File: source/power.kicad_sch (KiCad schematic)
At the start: 135 parts, among them Q1 MMBT5401, Q10 MMBT5401, Q11 CSD19536KCS, Q12 CSD19536KCS, Q2 MMBT5401, Q3 CSD19536KCS, Q4 CSD19536KCS, Q5 MMBT5401, Q6 MMBT5401, Q7 CSD19536KCS, Q8 CSD19536KCS, Q9 MMBT5401, U11 MS8311, U12 MS8311, U13 MS8311

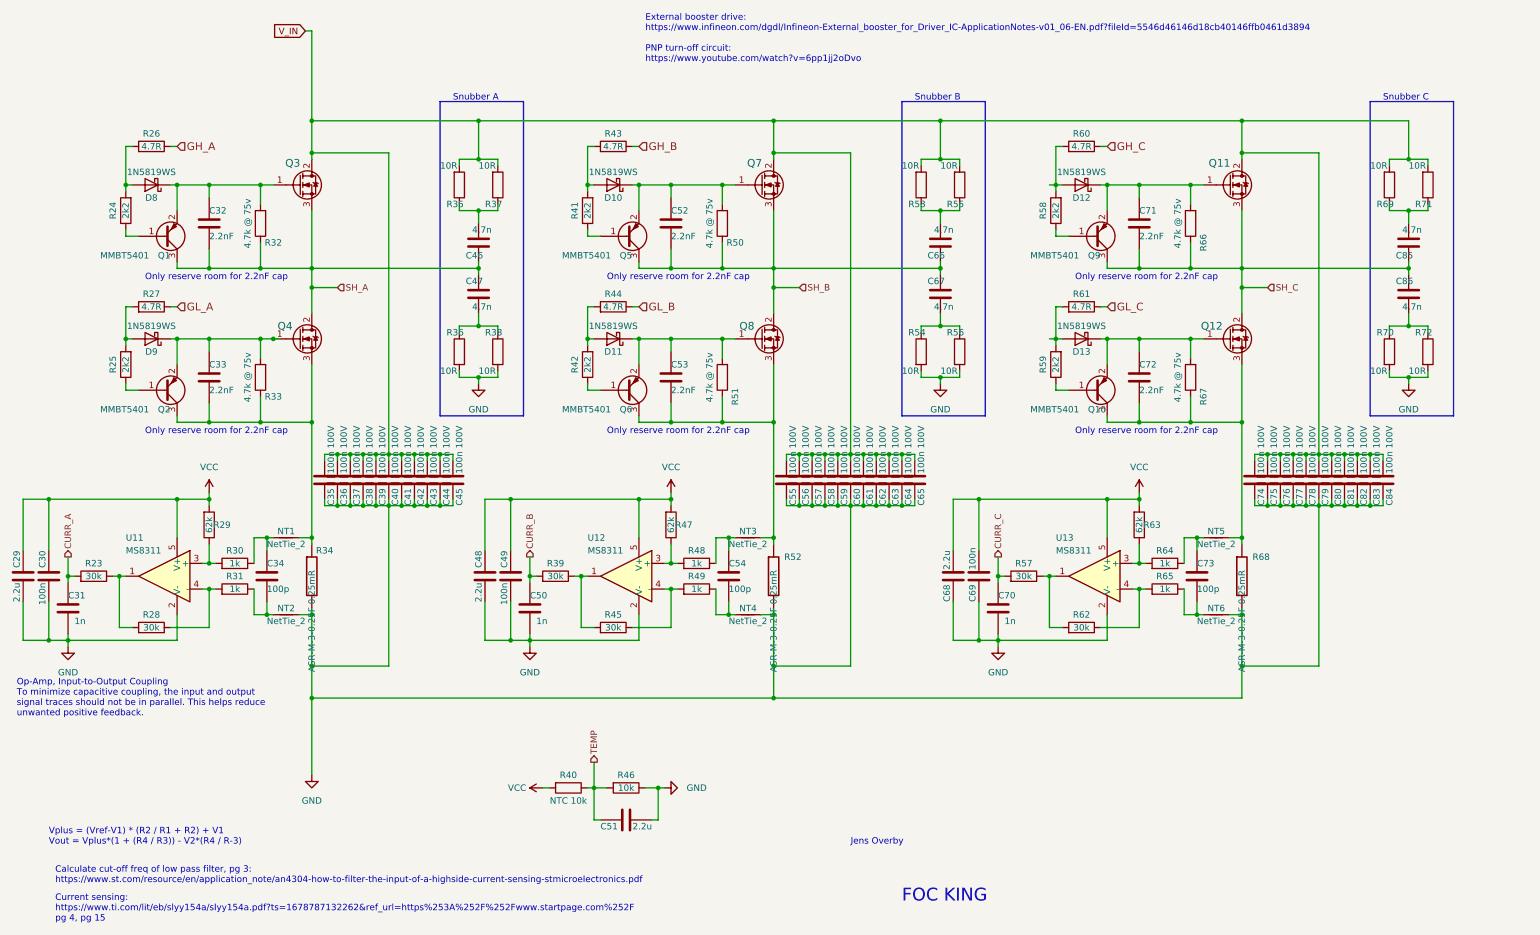
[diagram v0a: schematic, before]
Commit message: 4 layer design
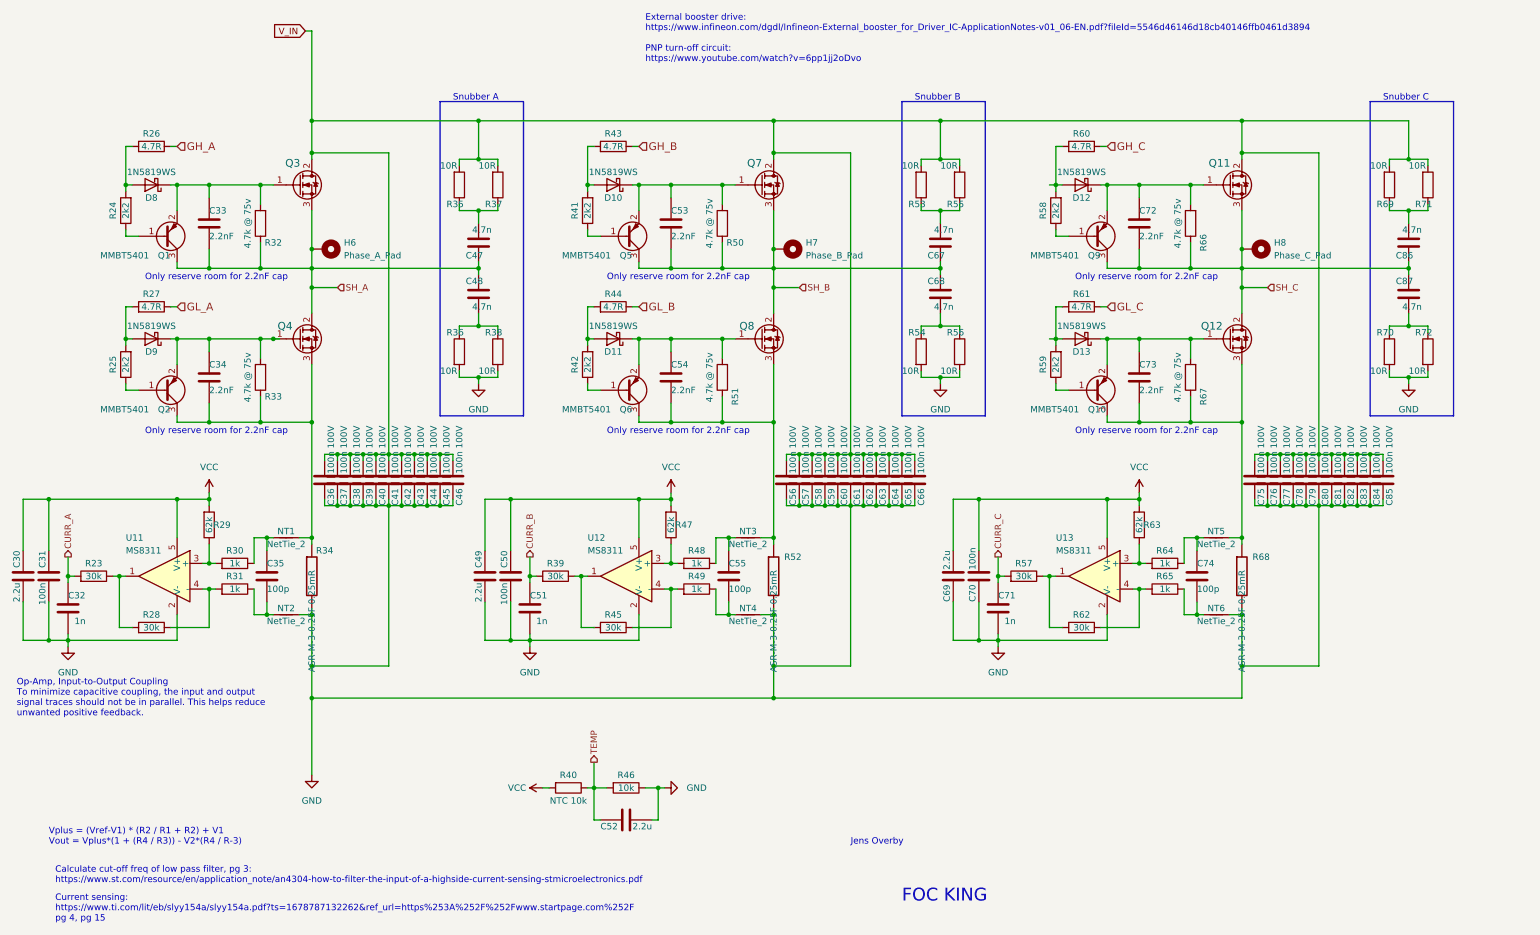
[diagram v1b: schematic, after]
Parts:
- added H6: Phase_A_Pad, Custom:MountingHole_3.5mm_Pad_TopOnly_custom, symbol Mechanical:MountingHole_Pad
- added H7: Phase_B_Pad, Custom:MountingHole_3.5mm_Pad_TopOnly_custom, symbol Mechanical:MountingHole_Pad
- added H8: Phase_C_Pad, Custom:MountingHole_3.5mm_Pad_TopOnly_custom, symbol Mechanical:MountingHole_Pad
- Q11, Q12, Q3, Q4, Q7, Q8: footprint Package_TO_SOT_THT:TO-220-3_Vertical -> Custom:TO-220-3_Vertical_bend
- renumbered C29 to C30, C30 to C31, C31 to C32, C32 to C33, C33 to C34, C34 to C35, C35 to C36, C36 to C37, C37 to C38, C38 to C39, C39 to C40, C40 to C41, C41 to C42, C42 to C43, C43 to C44, C44 to C45, C45 to C46, C46 to C47, C47 to C48, C48 to C49, C49 to C50, C50 to C51, C51 to C52, C52 to C53, C53 to C54, C54 to C55, C55 to C56, C56 to C57, C57 to C58, C58 to C59, C59 to C60, C60 to C61, C61 to C62, C62 to C63, C63 to C64, C64 to C65, C65 to C66, C66 to C67, C67 to C68, C68 to C69, C69 to C70, C70 to C71, C71 to C72, C72 to C73, C73 to C74, C74 to C75, C75 to C76, C76 to C77, C77 to C78, C78 to C79, C79 to C80, C80 to C81, C81 to C82, C82 to C83, C83 to C84, C84 to C85, C85 to C86, C86 to C87
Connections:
- net SH_A: now also H6.1
- net SH_B: now also H7.1
- net SH_C: now also H8.1

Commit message: Add files via upload
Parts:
- removed C33, C34, C53, C54, C72, C73: 2.2nF, Capacitor_SMD:C_0603_1608Metric, symbol BLDC_4-rescue:C-RESCUE-BLDC_4
- removed R32, R33, R50, R51, R66, R67: 4.7k @ 75v, Resistor_SMD:R_0603_1608Metric, symbol Device:R
- Q11, Q12, Q3, Q4, Q7, Q8: value CSD19536KCS -> CRST030N10N; footprint Custom:TO-220-3_Vertical_bend -> (none); LCSC (none) -> C841369
- R24: value 2k2 -> 0R; LCSC C22975 -> C21189
- R25: value 2k2 -> 2.2R; LCSC C22975 -> C22939
- R27: value 4.7R -> 2.2R; LCSC C23164 -> C22939
- R39: renamed from R41; value 2k2 -> 0R; LCSC C22975 -> C21189
- R40: renamed from R42; value 2k2 -> 2.2R; LCSC C22975 -> C22939
- R42: renamed from R44; value 4.7R -> 2.2R; LCSC C23164 -> C22939
- R54: renamed from R58; value 2k2 -> 0R; LCSC C22975 -> C21189
- R55: renamed from R59; value 2k2 -> 2.2R; LCSC C22975 -> C22939
- R57: renamed from R61; value 4.7R -> 2.2R; LCSC C23164 -> C22939
- renumbered C35 to C33, C36 to C34, C37 to C35, C38 to C36, C39 to C37, C40 to C38, C41 to C39, C42 to C40, C43 to C41, C44 to C42, C45 to C43, C46 to C44, C47 to C45, C48 to C46, C49 to C47, C50 to C48, C51 to C49, C52 to C50, C55 to C51, C56 to C52, C57 to C53, C58 to C54, C59 to C55, C60 to C56, C61 to C57, C62 to C58, C63 to C59, C64 to C60, C65 to C61, C66 to C62, C67 to C63, C68 to C64, C69 to C65, C70 to C66, C71 to C67, C74 to C68, C75 to C69, C76 to C70, C77 to C71, C78 to C72, C79 to C73, C80 to C74, C81 to C75, C82 to C76, C83 to C77, C84 to C78, C85 to C79, C86 to C80, C87 to C81, H6 to H5, H7 to H6, H8 to H7, R34 to R32, R35 to R33, R36 to R34, R37 to R35, R38 to R36, R39 to R37, R40 to R38, R43 to R41, R45 to R43, R46 to R44, R47 to R45, R48 to R46, R49 to R47, R52 to R48, R53 to R49, R54 to R50, R55 to R51, R56 to R52, R57 to R53, R60 to R56, R62 to R58, R63 to R59, R64 to R60, R65 to R61, R68 to R62, R69 to R63, R70 to R64, R71 to R65, R72 to R66
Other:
- note removed: "Only reserve room for 2.2nF cap"

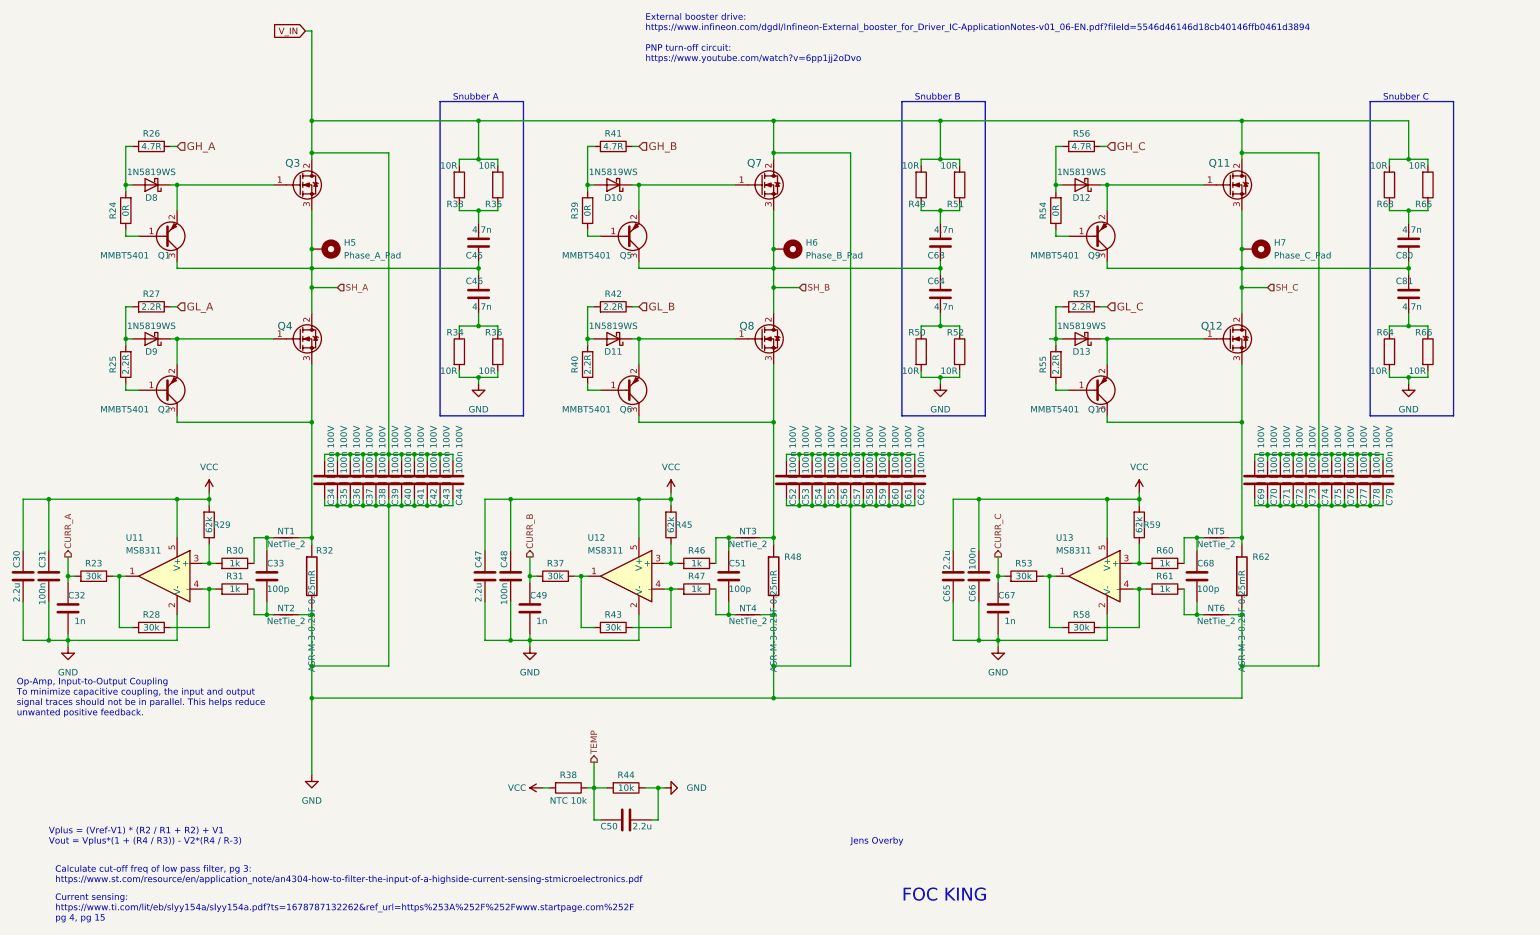
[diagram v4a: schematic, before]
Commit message: Add files via upload
Filter resistor on current op-amps changed from 30k to 150R
Mosfets at 45 deg angle
Changed layout of power supply
Cut through center of board
Unnecessary components near mosfets removed
Voltage filters removed again
Crystal suspected noise source - moved to back of board
Current sensing moved to in0 - in2 (PA0-PA2)
Voltage sensing moved to in11-in13
Supply voltage moved to in10
Mosfets can now be attached to heat-sink plate using screws (that can be tightened throug holes in the board)
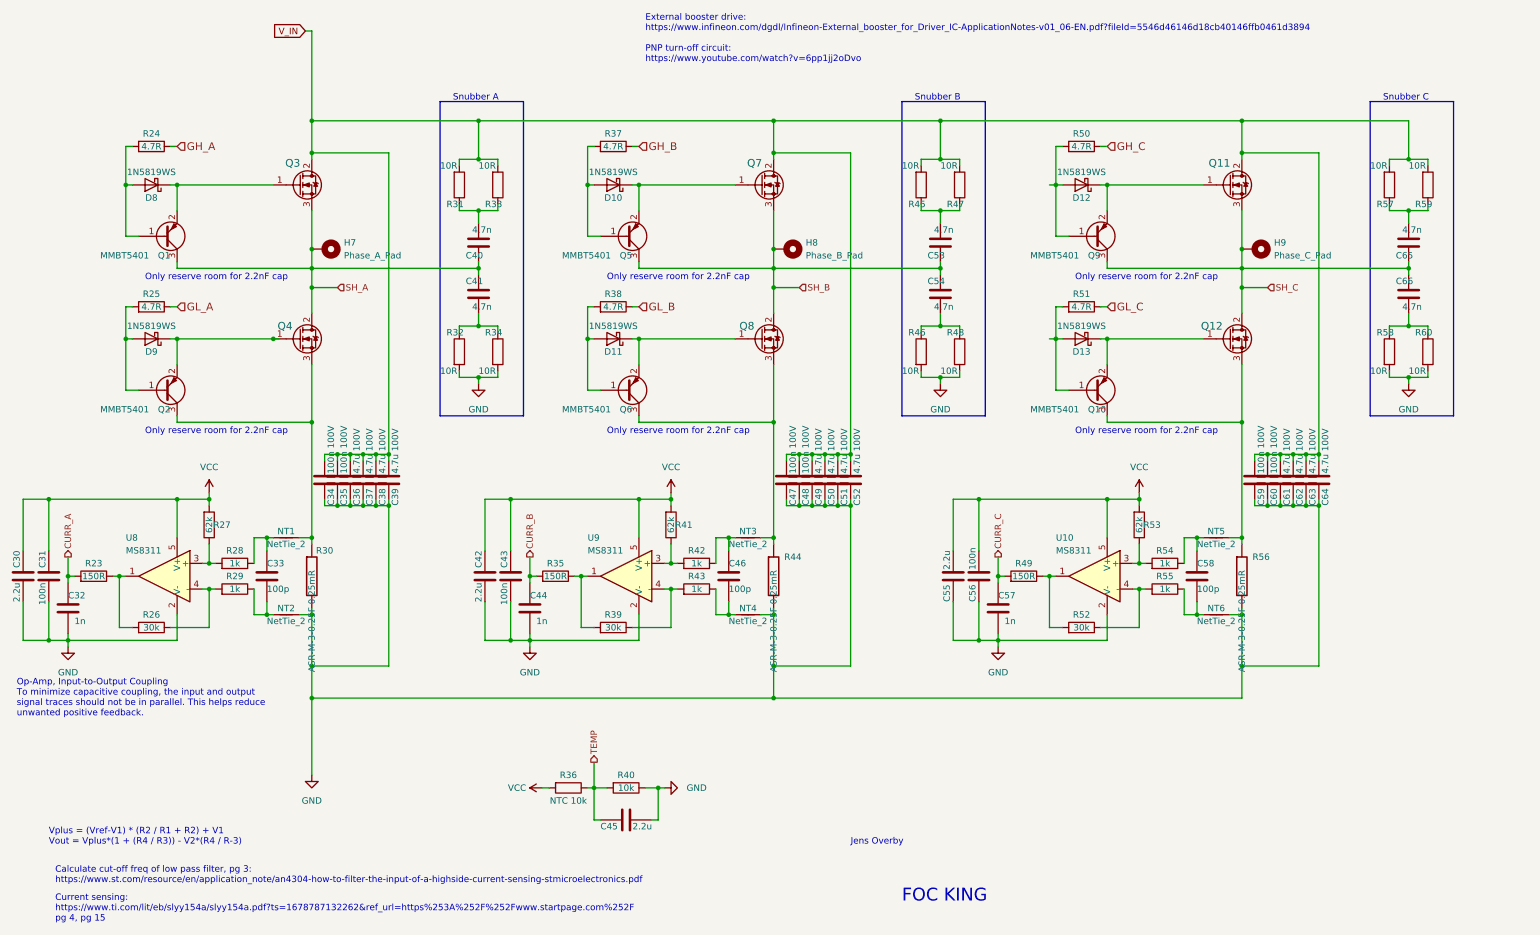
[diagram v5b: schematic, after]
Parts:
- removed C40, C41, C42, C43, C44, C53, C54, C55, C56, C57, C58, C69, C70, C71, C72, C73, C74, C75, C76, C77, C78, C79: 100n 100V, Capacitor_SMD:C_0805_2012Metric, symbol Device:C
- removed R24, R39, R54: 0R, Resistor_SMD:R_0603_1608Metric, symbol Device:R
- removed R25, R40, R55: 2.2R, Resistor_SMD:R_0603_1608Metric, symbol Device:R
- added C47, C48: 100n 100V, Capacitor_SMD:C_0805_2012Metric, symbol Device:C
- added C49, C50, C51, C63, C64: 4.7u 100V, Capacitor_SMD:C_1210_3225Metric, symbol Device:C
- C36, C37, C38, C39, C52, C61, C62: value 100n 100V -> 4.7u 100V; footprint Capacitor_SMD:C_0805_2012Metric -> Capacitor_SMD:C_1210_3225Metric; LRSC C28233 -> C381466
- Q11, Q12, Q3, Q4, Q7, Q8: value CRST030N10N -> CSD19536KCS; footprint (none) -> Custom:TO-220-3_Vertical_bend; LCSC C841369 -> (none)
- R23: value 30k -> 150R; LCSC C22984 -> C22808
- R25: renamed from R27; value 2.2R -> 4.7R; LCSC C22939 -> C23164
- R35: renamed from R37; value 30k -> 150R; LCSC C22984 -> C22808
- R38: renamed from R42; value 2.2R -> 4.7R; LCSC C22939 -> C23164
- R49: renamed from R53; value 30k -> 150R; LCSC C22984 -> C22808
- R51: renamed from R57; value 2.2R -> 4.7R; LCSC C22939 -> C23164
- renumbered C45 to C40, C46 to C41, C47 to C42, C48 to C43, C49 to C44, C50 to C45, C51 to C46, C63 to C53, C64 to C54, C65 to C55, C66 to C56, C67 to C57, C68 to C58, C80 to C65, C81 to C66, H5 to H7, H6 to H8, H7 to H9, R26 to R24, R28 to R26, R29 to R27, R30 to R28, R31 to R29, R32 to R30, R33 to R31, R34 to R32, R35 to R33, R36 to R34, R38 to R36, R41 to R37, R43 to R39, R44 to R40, R45 to R41, R46 to R42, R47 to R43, R48 to R44, R49 to R45, R50 to R46, R51 to R47, R52 to R48, R56 to R50, R58 to R52, R59 to R53, R60 to R54, R61 to R55, R62 to R56, R63 to R57, R64 to R58, R65 to R59, R66 to R60, U13 to U10, U11 to U8, U12 to U9
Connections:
- net GND: now also C47.2, C48.2, C49.2, C50.2, C51.2, C63.2, C64.2
- net V_IN: now also C47.1, C48.1, C49.1, C50.1, C51.1, C63.1, C64.1
- net at D10.2 (A), R37.2: now also Q5.1 (B)
- net at D8.2 (A), R24.2: now also Q1.1 (B)
- net at D11.2 (A), R38.2: now also Q6.1 (B)
- net at D12.2 (A), R50.2: now also Q9.1 (B)
- net at Q2.1 (B): now also D9.2 (A), R25.2
- net at D13.2 (A), R51.2: now also Q10.1 (B)
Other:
- note added: "Only reserve room for 2.2nF cap"

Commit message: 2 board setup with mcu and foc shield separated
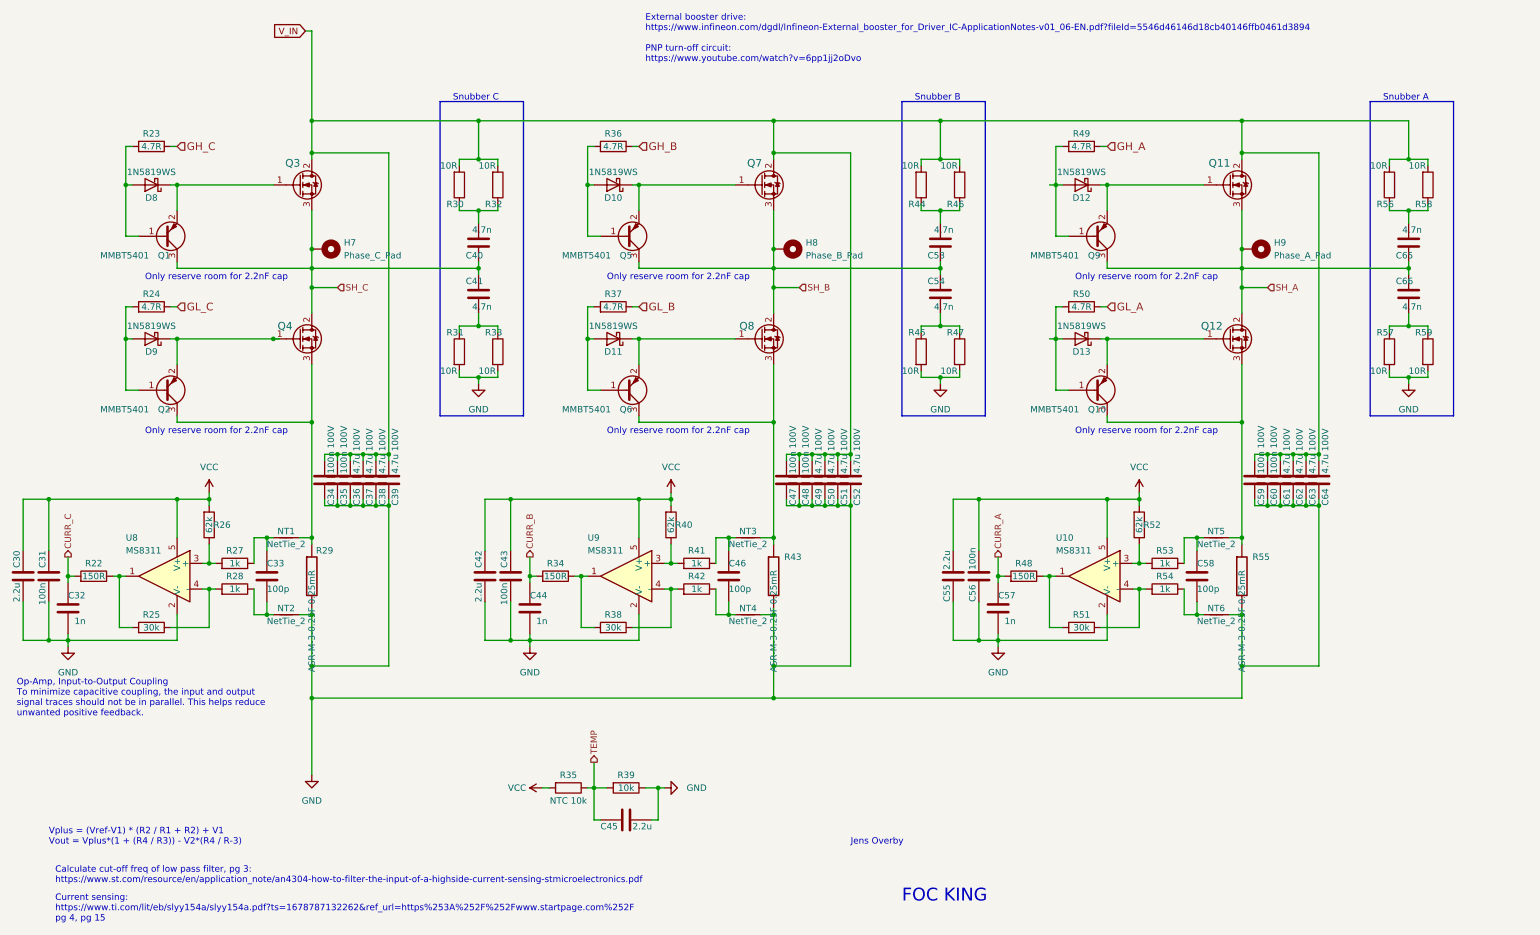
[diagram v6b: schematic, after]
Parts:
- H7: value Phase_A_Pad -> Phase_C_Pad
- H9: value Phase_C_Pad -> Phase_A_Pad
- renumbered R23 to R22, R24 to R23, R25 to R24, R26 to R25, R27 to R26, R28 to R27, R29 to R28, R30 to R29, R31 to R30, R32 to R31, R33 to R32, R34 to R33, R35 to R34, R36 to R35, R37 to R36, R38 to R37, R39 to R38, R40 to R39, R41 to R40, R42 to R41, R43 to R42, R44 to R43, R45 to R44, R46 to R45, R47 to R46, R48 to R47, R49 to R48, R50 to R49, R51 to R50, R52 to R51, R53 to R52, R54 to R53, R55 to R54, R56 to R55, R57 to R56, R58 to R57, R59 to R58, R60 to R59
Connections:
- net CURR_A: now also C57.2, R48.2; no longer C32.2, R22.2
- net CURR_C: now also C32.2, R22.2; no longer C57.2, R48.2
- net GH_A: now also R49.1; no longer R23.1
- net GH_C: now also R23.1; no longer R49.1
- net GL_A: now also R50.1; no longer R24.1
- net GL_C: now also R24.1; no longer R50.1
- net SH_A: now also C65.1, C66.1, H9.1, Q11.3 (S), Q12.2 (D), Q9.3 (C); no longer C40.1, C41.1, H7.1, Q1.3 (C), Q3.3 (S), Q4.2 (D)
- net SH_C: now also C40.1, C41.1, H7.1, Q1.3 (C), Q3.3 (S), Q4.2 (D); no longer C65.1, C66.1, H9.1, Q11.3 (S), Q12.2 (D), Q9.3 (C)
